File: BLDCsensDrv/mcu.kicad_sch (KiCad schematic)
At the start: 31 parts, among them J20 Utility Pins, J23 DB9_Female, Q20 BC556, Q21 BC548, SW1 RESET, U2 STM32G030K6T6

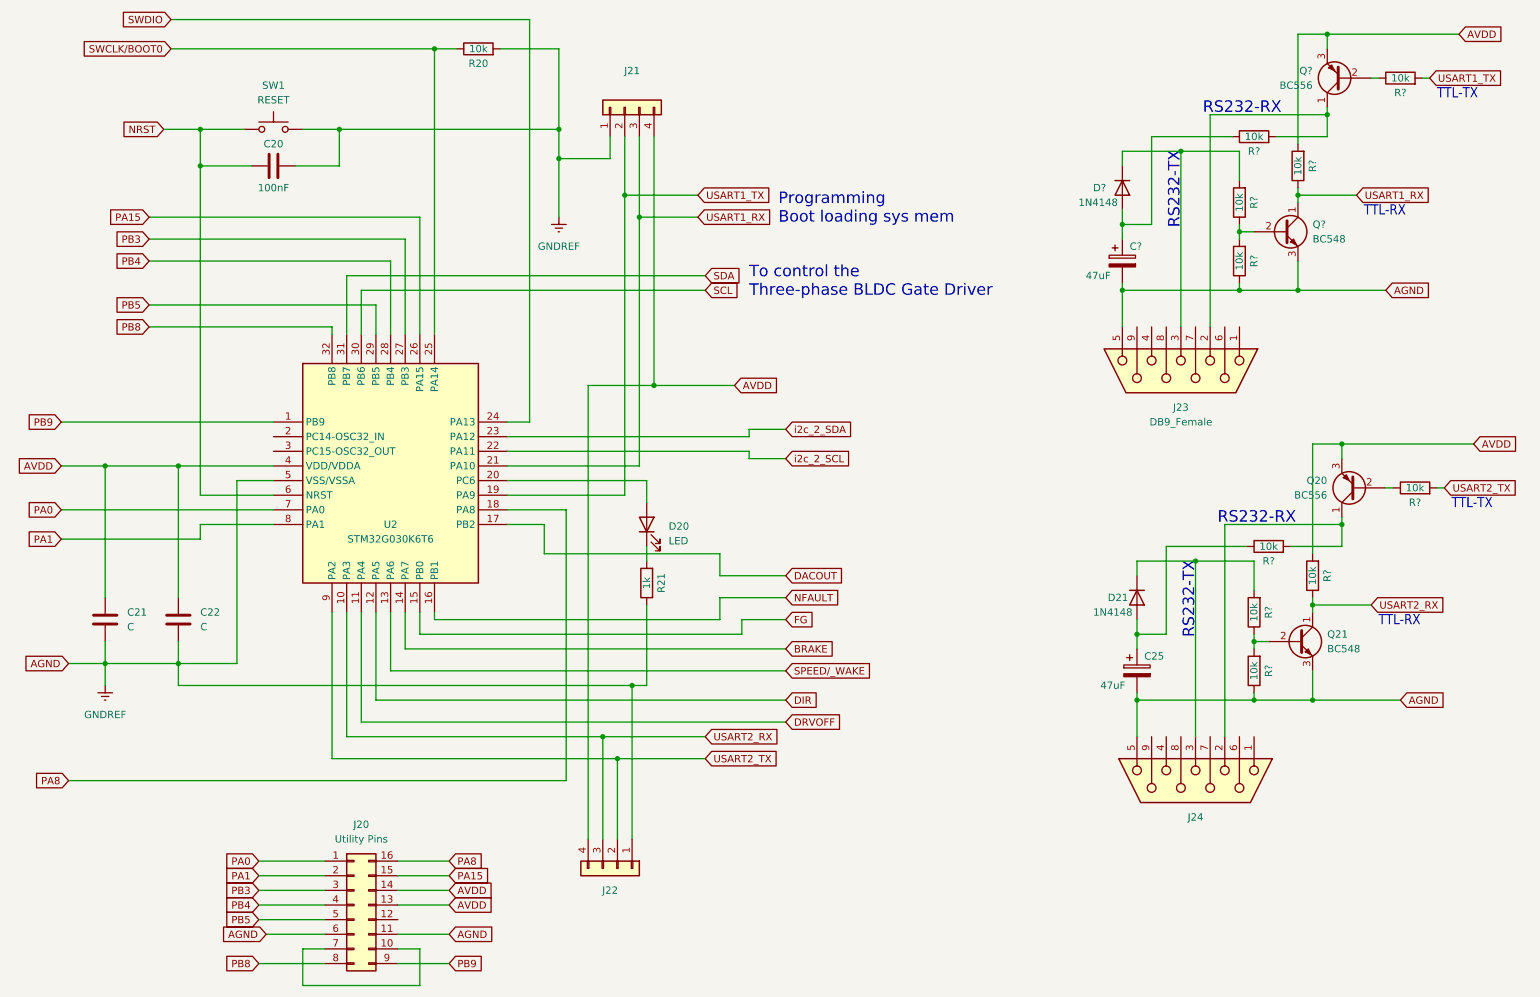
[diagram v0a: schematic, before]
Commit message: 3-phase Trapezoidal Control hardware ready for prototype prod.
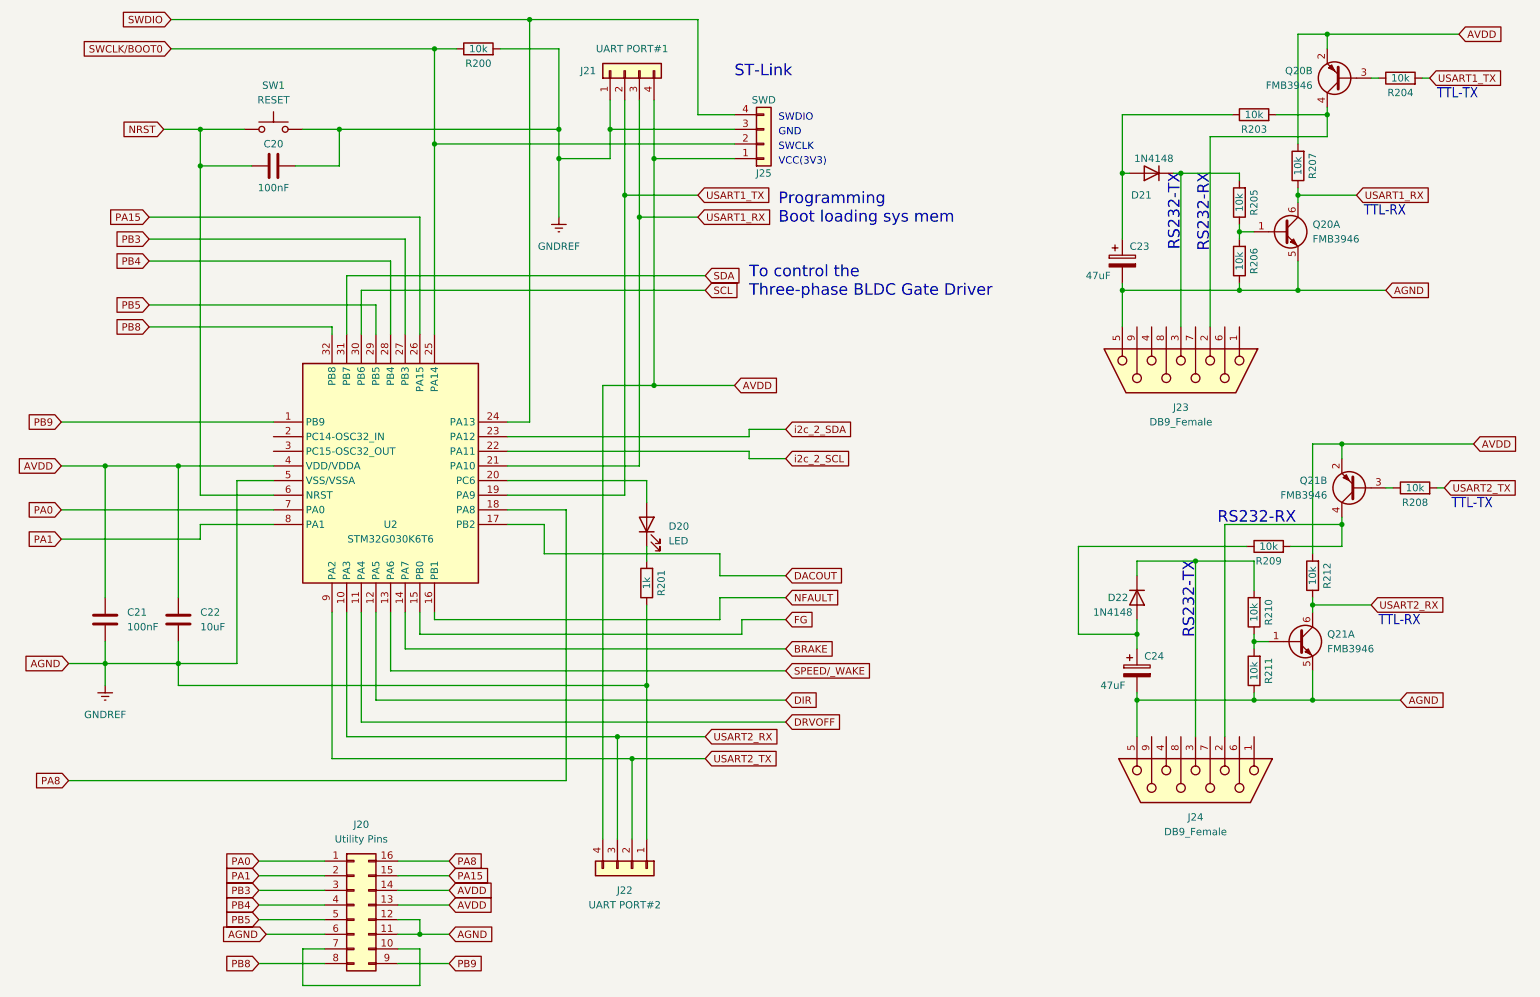
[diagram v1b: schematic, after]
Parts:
- removed D?: 1N4148, Diode_THT:D_DO-35_SOD27_P7.62mm_Horizontal, symbol Diode:1N4148
- removed Q20, Q?: BC556, Package_TO_SOT_THT:TO-92_Inline, symbol Transistor_BJT:BC556
- removed Q21, Q?: BC548, Package_TO_SOT_THT:TO-92_Inline, symbol Transistor_BJT:BC548
- added D21: 1N4148, Diode_SMD:D_1206_3216Metric_Pad1.42x1.75mm_HandSolder, symbol Diode:1N4148
- added J25: SWD, Connector_PinHeader_2.54mm:PinHeader_1x04_P2.54mm_Vertical, symbol Connector_Generic:Conn_01x04
- added Q20, Q21: FMB3946, Package_TO_SOT_SMD:TSOT-23-6_HandSoldering, symbol Transistor_BJT:FMB3946
- C20: footprint (none) -> Capacitor_SMD:C_0805_2012Metric_Pad1.18x1.45mm_HandSolder
- C21: value C -> 100nF; footprint (none) -> Capacitor_SMD:C_0805_2012Metric_Pad1.18x1.45mm_HandSolder
- C22: value C -> 10uF; footprint (none) -> Capacitor_SMD:C_1206_3216Metric_Pad1.33x1.80mm_HandSolder
- C23: renamed from C?; footprint (none) -> Capacitor_SMD:C_1206_3216Metric_Pad1.33x1.80mm_HandSolder
- C24: renamed from C25; footprint (none) -> Capacitor_SMD:C_1206_3216Metric_Pad1.33x1.80mm_HandSolder
- D20: footprint (none) -> LED_SMD:LED_1206_3216Metric_Pad1.42x1.75mm_HandSolder
- D22: renamed from D21; footprint Diode_THT:D_DO-35_SOD27_P7.62mm_Horizontal -> Diode_SMD:D_1206_3216Metric_Pad1.42x1.75mm_HandSolder
- J20: footprint (none) -> Connector_PinHeader_2.54mm:PinHeader_2x08_P2.54mm_Vertical
- J21: value (none) -> UART PORT#1; footprint (none) -> Connector_PinHeader_2.54mm:PinHeader_1x04_P2.54mm_Vertical
- J22: value (none) -> UART PORT#2; footprint (none) -> Connector_PinHeader_2.54mm:PinHeader_1x04_P2.54mm_Vertical
- J23: footprint (none) -> Connector_Dsub:DSUB-9_Female_Horizontal_P2.77x2.84mm_EdgePinOffset9.90mm_Housed_MountingHolesOffset11.32mm
- J24: value (none) -> DB9_Female; footprint (none) -> Connector_Dsub:DSUB-9_Female_Horizontal_P2.77x2.84mm_EdgePinOffset9.90mm_Housed_MountingHolesOffset11.32mm
- R200: renamed from R20; footprint Resistor_THT:R_Axial_DIN0207_L6.3mm_D2.5mm_P10.16mm_Horizontal -> Resistor_SMD:R_1206_3216Metric_Pad1.30x1.75mm_HandSolder
- R201: renamed from R21; footprint Resistor_THT:R_Axial_DIN0207_L6.3mm_D2.5mm_P10.16mm_Horizontal -> Resistor_SMD:R_1206_3216Metric_Pad1.30x1.75mm_HandSolder
- R203, R204, R205, R206, R207, R208, R209, R210, R211, R212: renamed from R?; footprint Resistor_THT:R_Axial_DIN0207_L6.3mm_D2.5mm_P10.16mm_Horizontal -> Resistor_SMD:R_1206_3216Metric_Pad1.30x1.75mm_HandSolder
- SW1: footprint (none) -> Button_Switch_THT:SW_PUSH_6mm_H5mm
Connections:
- net AVDD: now also J25.1 (Pin_1), Q20.2 (E2), Q21.2 (E2)
- net GNDREF: now also J20.12 (Pin_12), J25.3 (Pin_3), Q20.5 (E1), Q21.5 (E1)
- net SWCLK/BOOT0: now also J25.2 (Pin_2)
- net SWDIO: now also J25.4 (Pin_4)
- net USART1_RX: now also Q20.6 (C1)
- net USART2_RX: now also Q21.6 (C1)
- net at C23.1, R203.1: now also D21.2 (A)
- net at R210.1, R211.2: now also Q21.1 (B1)
- net at R205.1, R206.2: now also Q20.1 (B1)
- net at J23.2, R203.2: now also Q20.4 (C2)
- net at J23.3, R205.2: now also D21.1 (K)
- net at R208.1: now also Q21.3 (B2)
- net at J24.2, R209.2: now also Q21.4 (C2)
- net at R204.1: now also Q20.3 (B2)
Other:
- note added: "GND"
- note added: "ST-Link"
- note added: "SWCLK"
- note added: "SWDIO"
- note added: "VCC(3V3)"
- moved on the sheet: J21, J22, R203
